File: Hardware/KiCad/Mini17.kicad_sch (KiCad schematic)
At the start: 0 parts

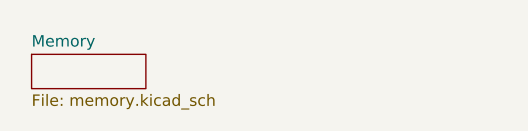
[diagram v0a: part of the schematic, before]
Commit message: many edits throughout, added board edges for main & HMI combined, added rough layouts for some components on both
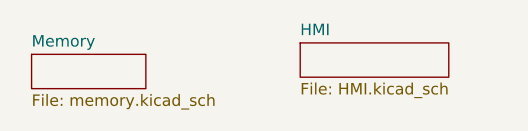
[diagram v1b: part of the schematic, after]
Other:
- added sheet HMI (HMI.kicad_sch)
